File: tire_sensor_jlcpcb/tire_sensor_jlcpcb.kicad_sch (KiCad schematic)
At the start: 40 parts, among them J1 Conn_02x05_Odd_Even, U2 DPS368, U3 LIS3DHTR, X1 32MHz, X2 32.768kHz

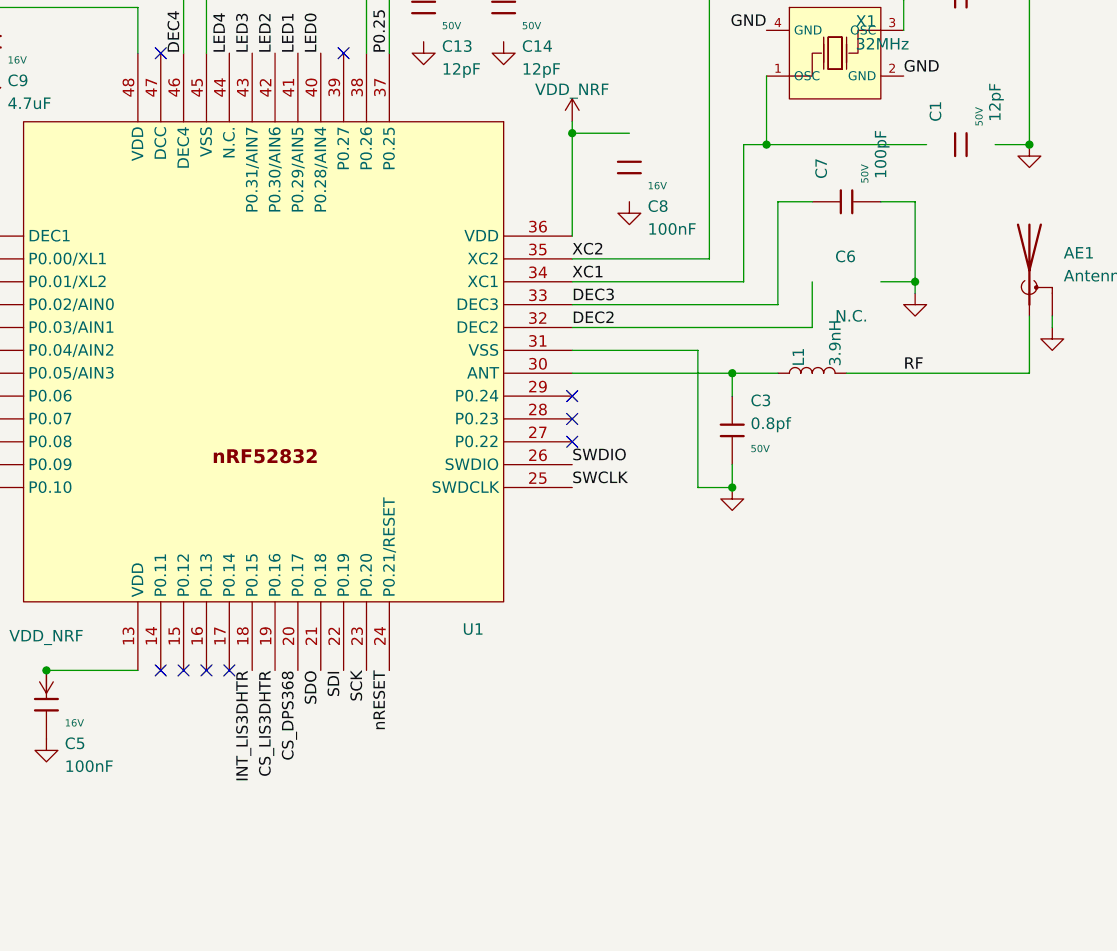
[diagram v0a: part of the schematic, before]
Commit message: Better routing and decoupling, reomved unused cap
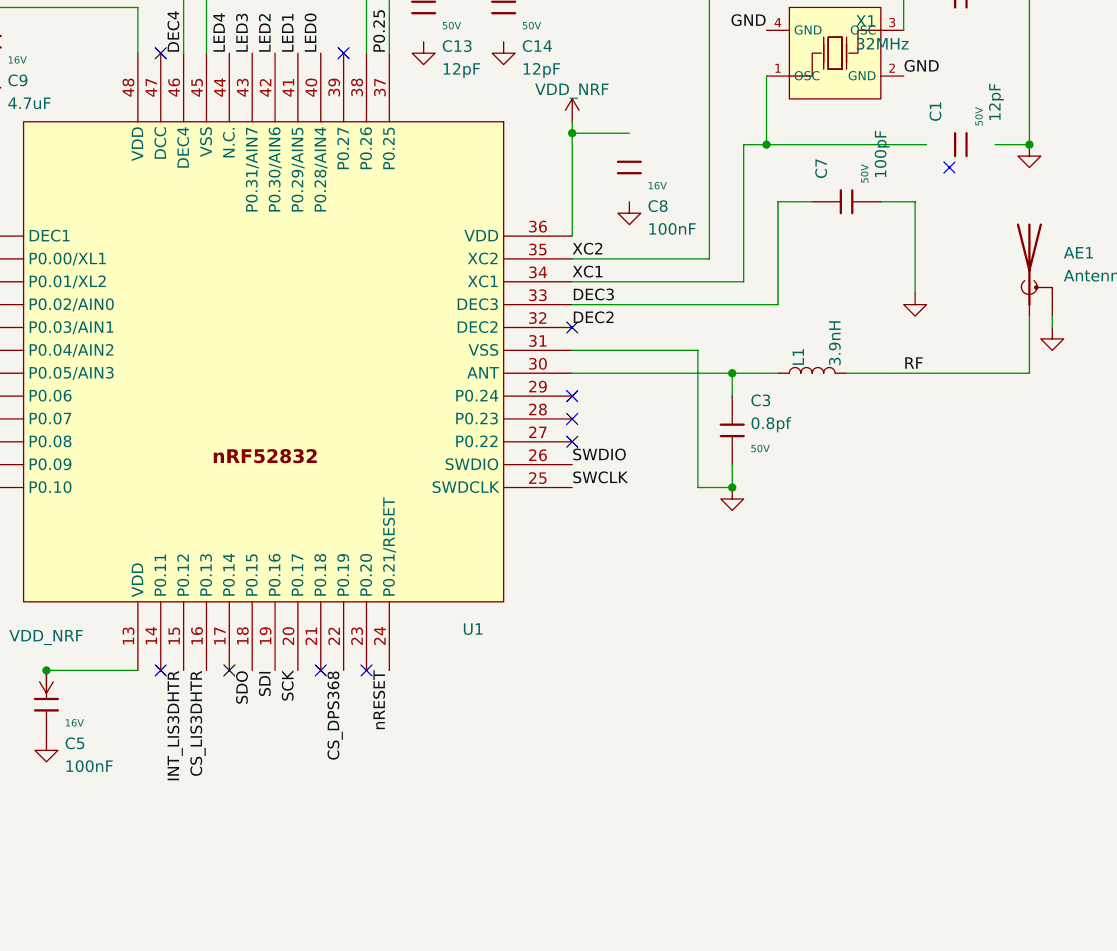
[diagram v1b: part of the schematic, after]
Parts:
- removed C6: N.C., Capacitor_SMD:C_0402_1005Metric, symbol temp_sensor_2-altium-import:root_2_CAP_Nordic Passive DB.DbLib
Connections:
- net CS_DPS368: now also U1.22 (P0.19); no longer U1.20 (P0.17)
- net CS_LIS3DHTR: now also U1.16 (P0.13); no longer U1.19 (P0.16)
- net INT_LIS3DHTR: now also U1.15 (P0.12); no longer U1.18 (P0.15)
- net SCK: now also U1.20 (P0.17); no longer U1.23 (P0.20)
- net SDI: now also U1.19 (P0.16); no longer U1.22 (P0.19)
- net SDO: now also U1.18 (P0.15); no longer U1.21 (P0.18)
- no-connect marks 23 -> 25

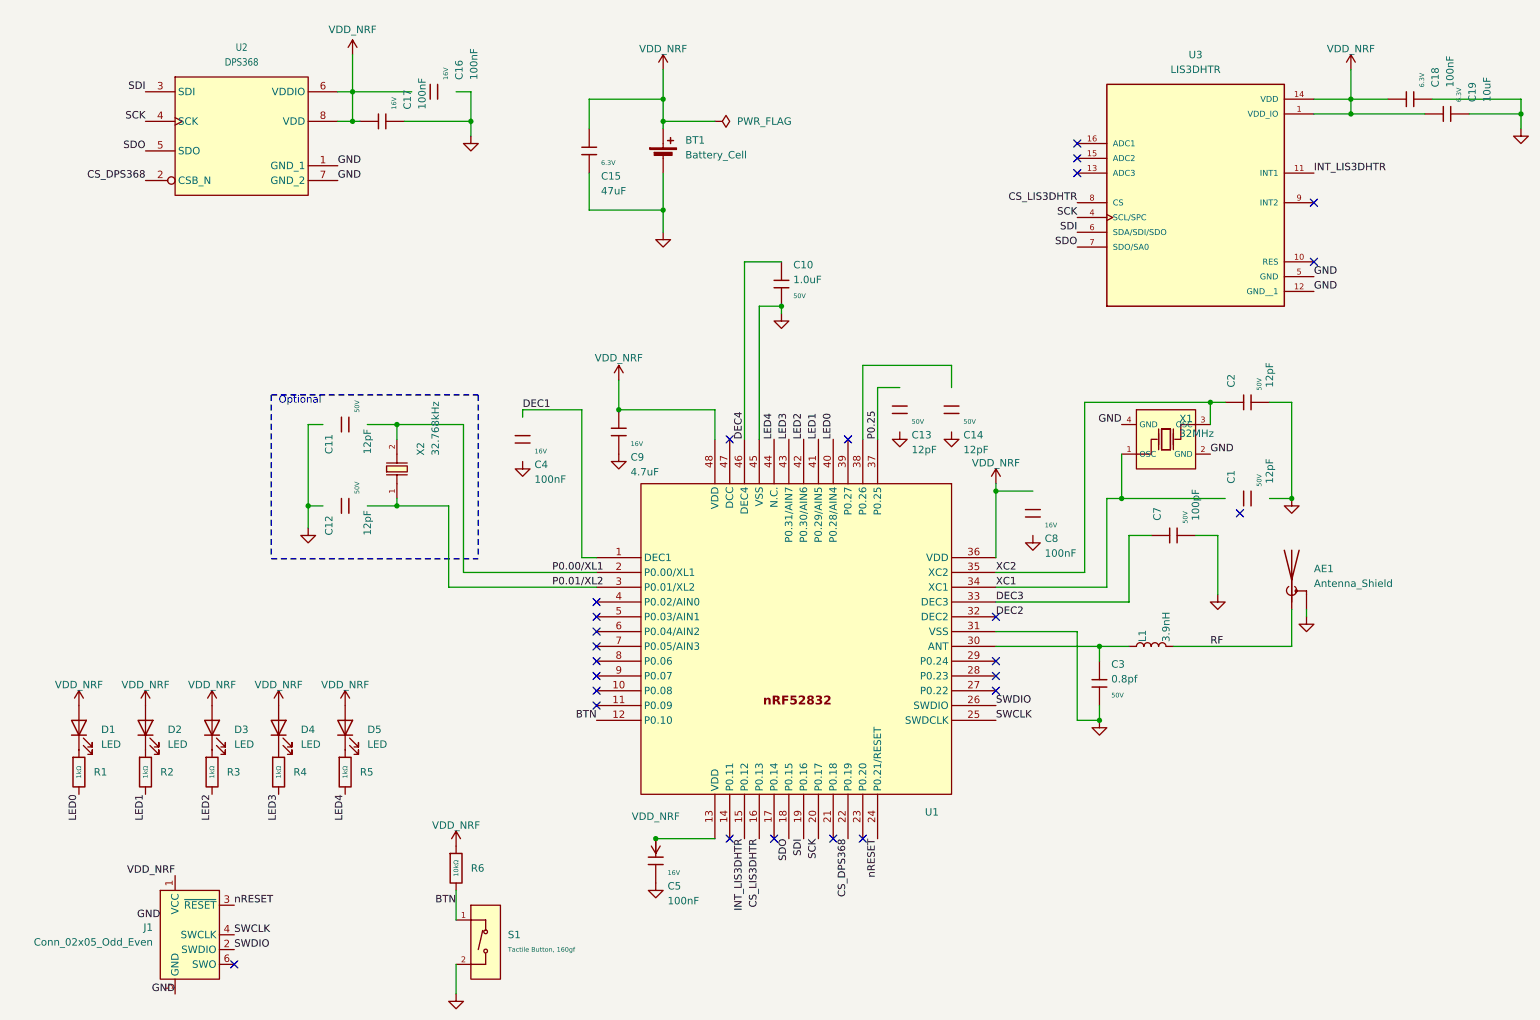
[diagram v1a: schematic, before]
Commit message: Add gyro, reroute sensors
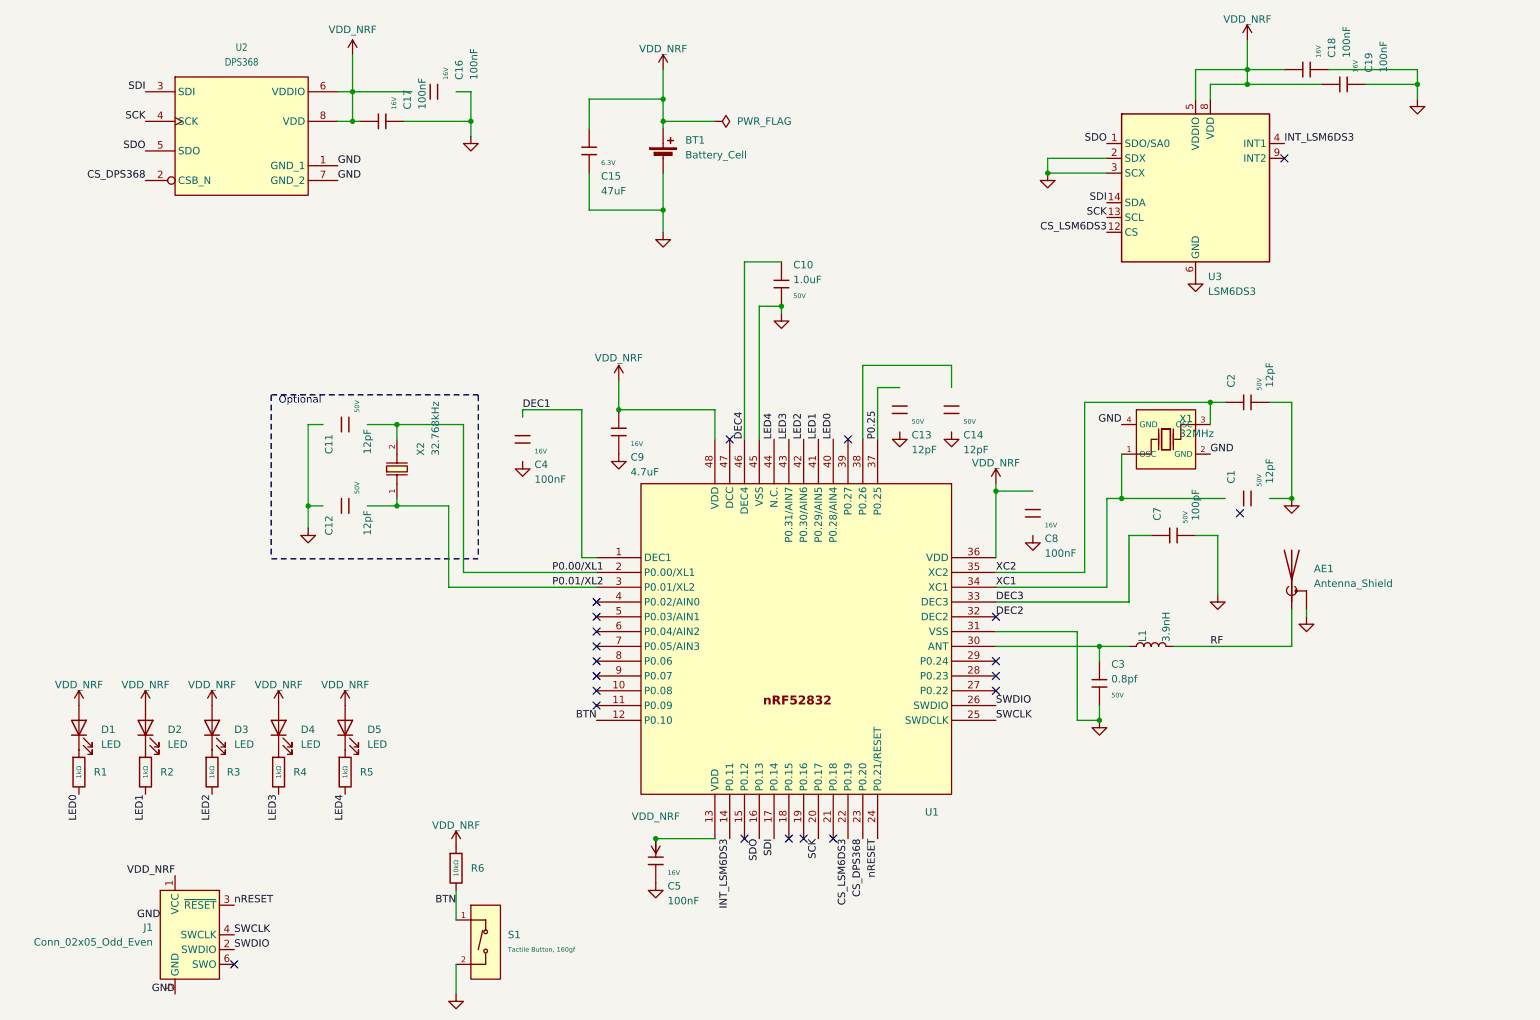
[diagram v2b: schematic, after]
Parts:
- C19: value 10uF -> 100nF; symbol PCM_JLCPCB-Capacitors:0402,10uF -> PCM_JLCPCB-Capacitors:0402,100nF; Capacitance 10uF -> 100nF; LCSC C15525 -> C1525; Part CL05A106MQ5NUNC -> CL05B104KO5NNNC; Price 0.009USD -> 0.004USD; Stock 2142015 -> 18435590; Temperature Coefficient X5R -> X7R; Tolerance ±20% -> ±10%; Voltage Rated 6.3V -> 16V
- U3: value LIS3DHTR -> LSM6DS3; footprint footprints:XDCR_LIS3DHTR -> Package_LGA:LGA-14_3x2.5mm_P0.5mm_LayoutBorder3x4y; symbol LIS3DHTR:LIS3DHTR -> Sensor_Motion:LSM6DS3
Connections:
- net CS_DPS368: now also U1.23 (P0.20); no longer U1.22 (P0.19)
- net GND: now also U3.2 (SDX), U3.3 (SCX), U3.6 (GND), U3.7 (GND); no longer U3.12 (GND__1), U3.5 (GND)
- net SCK: now also U3.13 (SCL); no longer U3.4 (SCL/SPC)
- net SDI: now also U1.17 (P0.14), U3.14 (SDA); no longer U1.19 (P0.16), U3.6 (SDA/SDI/SDO)
- net SDO: now also U1.16 (P0.13), U3.1 (SDO/SA0); no longer U1.18 (P0.15), U3.7 (SDO/SA0)
- net VDD_NRF: now also U3.5 (VDDIO), U3.8 (VDD); no longer U3.1 (VDD_IO), U3.14 (VDD)
- net INT_LSM6DS3: now reaches U1.14 (P0.11)
- net INT_LSM6DS3: now also U3.4 (INT1)
- removed net CS_LIS3DHTR: U1.16 (P0.13), U3.8 (CS)
- net INT_LIS3DHTR: no longer names the net of U3.11 (NC)
- net INT_LIS3DHTR: no longer U1.15 (P0.12)
- new net CS_LSM6DS3: U1.22 (P0.19), U3.12 (CS)
- no-connect marks 25 -> 21
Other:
- moved on the sheet: C18, C19
